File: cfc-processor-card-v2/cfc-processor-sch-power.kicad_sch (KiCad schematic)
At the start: 91 parts, among them Q1 DMP2240UDM, Q2 PMV45EN, Q3 DMP3050LVT-7, Q4 DMP3050LVT-7, Q5 PMV45EN, U1 MAX7310ATE+, U2 MIC842LYC5, U3 MIC842LYC5, U4 TS5A21366, U5 MAX4211FETE, U6 TPS62112

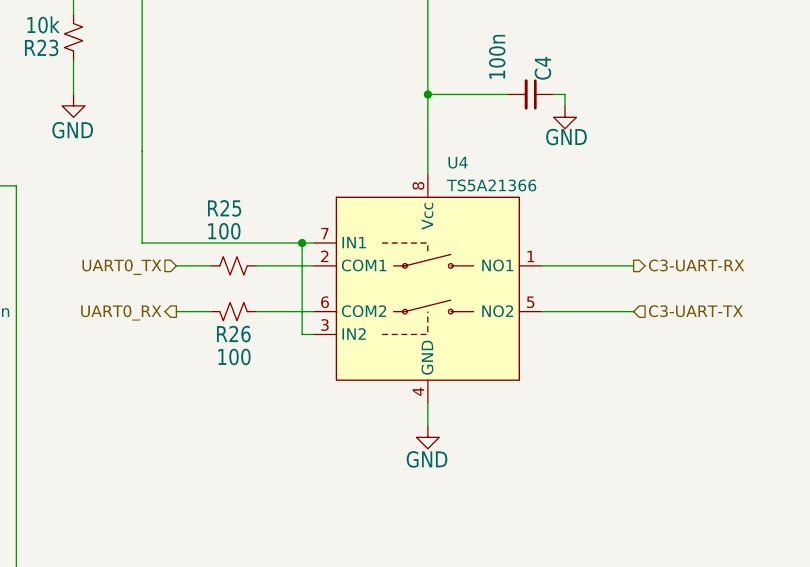
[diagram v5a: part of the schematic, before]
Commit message: Update
Changed passive component footprints to 0603 no silk c. Fixed OPD UART termination resistor on cfc processor card. Added low temp co and tolerance resistor for NTC  thermistor tec voltage divider.
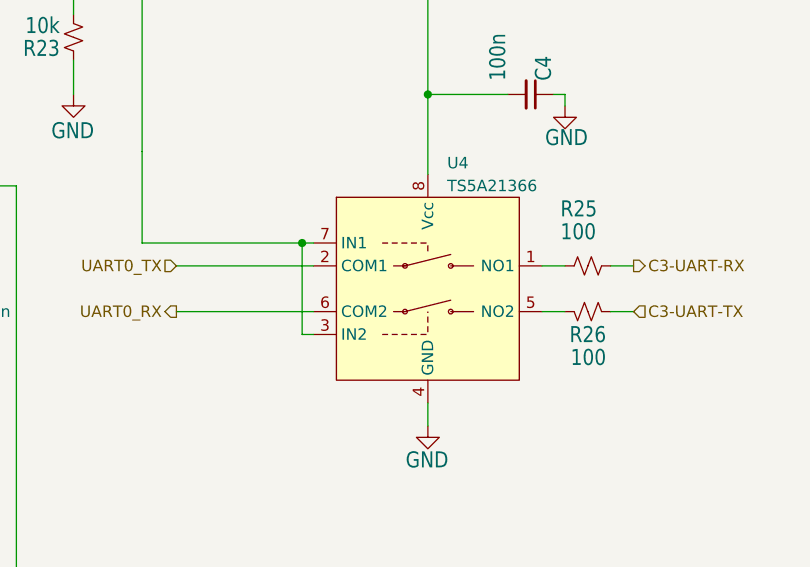
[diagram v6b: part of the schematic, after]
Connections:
- net C3-UART-RX: now also R25.1; no longer U4.1 (NO1)
- net C3-UART-TX: now also R26.2; no longer U4.5 (NO2)
- net UART0_RX: now also U4.6 (COM2); no longer R26.1
- net UART0_TX: now also U4.2 (COM1); no longer R25.2
- new net: R25.2, U4.1 (NO1)
- new net: R26.1, U4.5 (NO2)
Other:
- moved on the sheet: R25, R26
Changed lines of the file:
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@@
 	(wire
 		(pts
+			(xy 226.06 168.91) (xy 228.6 168.91)
+		)
+		(stroke
+			(width 0)
+			(type default)
+		)
+	)
+	(wire
+		(pts
 			(xy 68.58 48.26) (xy 71.12 48.26)
 		)
@@
 	(wire
 		(pts
+			(xy 226.06 173.99) (xy 228.6 173.99)
+		)
+		(stroke
+			(width 0)
+			(type default)
+		)
+	)
+	(wire
+		(pts
 			(xy 358.14 50.8) (xy 365.76 50.8)
 		)
@@
 	(wire
 		(pts
-			(xy 186.69 168.91) (xy 193.04 168.91)
-		)
-		(stroke
-			(width 0)
-			(type default)
-		)
-	)
-	(wire
-		(pts
 			(xy 320.04 60.96) (xy 332.74 60.96)
 		)
@@
 	(wire
 		(pts
-			(xy 186.69 173.99) (xy 193.04 173.99)
-		)
-		(stroke
-			(width 0)
-			(type default)
-		)
-	)
-	(wire
-		(pts
 			(xy 340.36 60.96) (xy 342.9 60.96)
 		)
@@
 	(wire
 		(pts
-			(xy 218.44 173.99) (xy 228.6 173.99)
+			(xy 177.8 173.99) (xy 193.04 173.99)
+		)
+		(stroke
+			(width 0)
+			(type default)
+		)
+	)
+	(wire
+		(pts
+			(xy 218.44 173.99) (xy 220.98 173.99)
 		)
 		(stroke
@@
 	(wire
 		(pts
-			(xy 177.8 168.91) (xy 181.61 168.91)
-		)
-		(stroke
-			(width 0)
-			(type default)
-		)
-	)
-	(wire
-		(pts
 			(xy 298.45 191.77) (xy 298.45 201.93)
 		)
@@
 	(wire
 		(pts
-			(xy 218.44 168.91) (xy 228.6 168.91)
+			(xy 218.44 168.91) (xy 220.98 168.91)
 		)
 		(stroke
@@
 	(wire
 		(pts
-			(xy 177.8 173.99) (xy 181.61 173.99)
-		)
-		(stroke
-			(width 0)
-			(type default)
-		)
-	)
-	(wire
-		(pts
 			(xy 283.21 59.69) (xy 283.21 53.34)
 		)
@@
 	(wire
 		(pts
+			(xy 177.8 168.91) (xy 193.04 168.91)
+		)
+		(stroke
+			(width 0)
+			(type default)
+		)
+	)
+	(wire
+		(pts
 			(xy 259.08 66.04) (xy 259.08 67.31)
 		)
@@
 	(symbol
 		(lib_id "Device:R_Small_US")
-		(at 184.15 173.99 90)
+		(at 223.52 173.99 90)
 		(mirror x)
 		(unit 1)
@@
 		(dnp no)
 		(property "Reference" "R26"
-			(at 186.182 175.514 90)
+			(at 225.552 175.514 90)
 			(show_name no)
 			(do_not_autoplace no)
@@
 		)
 		(property "Value" "100"
-			(at 186.182 178.054 90)
+			(at 225.552 178.054 90)
 			(show_name no)
 			(do_not_autoplace no)
@@
 		)
 		(property "Footprint" "oresat-passives:0603-C-NOSILK"
-			(at 184.15 173.99 0)
+			(at 223.52 173.99 0)
 			(hide yes)
 			(show_name no)
@@
 		)
 		(property "Datasheet" "https://www.seielect.com/catalog/sei-rmcf_rmcp.pdf"
-			(at 184.15 173.99 0)
+			(at 223.52 173.99 0)
 			(hide yes)
 			(show_name no)
@@
 		)
 		(property "Description" "Resistor, small US symbol"
-			(at 184.15 173.99 0)
+			(at 223.52 173.99 0)
 			(hide yes)
 			(show_name no)
@@
 		)
 		(property "DIS" "DigiKey"
-			(at 184.15 173.99 90)
+			(at 223.52 173.99 90)
 			(hide yes)
 			(show_name no)
@@
 		)
 		(property "DPN" "RMCF0603FT100RCT-ND"
-			(at 184.15 173.99 90)
+			(at 223.52 173.99 90)
 			(hide yes)
 			(show_name no)
@@
 		)
 		(property "MFR" "Stackpole Electronics Inc"
-			(at 184.15 173.99 90)
+			(at 223.52 173.99 90)
 			(hide yes)
 			(show_name no)
@@
 		)
 		(property "MPN" "RMCF0603FT100R"
-			(at 184.15 173.99 90)
+			(at 223.52 173.99 90)
 			(hide yes)
 			(show_name no)
@@
 	(symbol
 		(lib_id "Device:R_Small_US")
-		(at 184.15 168.91 270)
+		(at 223.52 168.91 270)
 		(unit 1)
 		(body_style 1)
@@
 		(dnp no)
 		(property "Reference" "R25"
-			(at 181.102 161.544 90)
+			(at 220.472 161.544 90)
 			(show_name no)
 			(do_not_autoplace no)
@@
 		)
 		(property "Value" "100"
-			(at 181.102 164.084 90)
+			(at 220.472 164.084 90)
 			(show_name no)
 			(do_not_autoplace no)
@@
 		)
 		(property "Footprint" "oresat-passives:0603-C-NOSILK"
-			(at 184.15 168.91 0)
+			(at 223.52 168.91 0)
 			(hide yes)
 			(show_name no)
@@
 		)
 		(property "Datasheet" "https://www.seielect.com/catalog/sei-rmcf_rmcp.pdf"
-			(at 184.15 168.91 0)
+			(at 223.52 168.91 0)
 			(hide yes)
 			(show_name no)
@@
 		)
 		(property "Description" "Resistor, small US symbol"
-			(at 184.15 168.91 0)
+			(at 223.52 168.91 0)
 			(hide yes)
 			(show_name no)
@@
 		)
 		(property "DIS" "DigiKey"
-			(at 184.15 168.91 90)
+			(at 223.52 168.91 90)
 			(hide yes)
 			(show_name no)
@@
 		)
 		(property "DPN" "RMCF0603FT100RCT-ND"
-			(at 184.15 168.91 90)
+			(at 223.52 168.91 90)
 			(hide yes)
 			(show_name no)
@@
 		)
 		(property "MFR" "Stackpole Electronics Inc"
-			(at 184.15 168.91 90)
+			(at 223.52 168.91 90)
 			(hide yes)
 			(show_name no)
@@
 		)
 		(property "MPN" "RMCF0603FT100R"
-			(at 184.15 168.91 90)
+			(at 223.52 168.91 90)
 			(hide yes)
 			(show_name no)

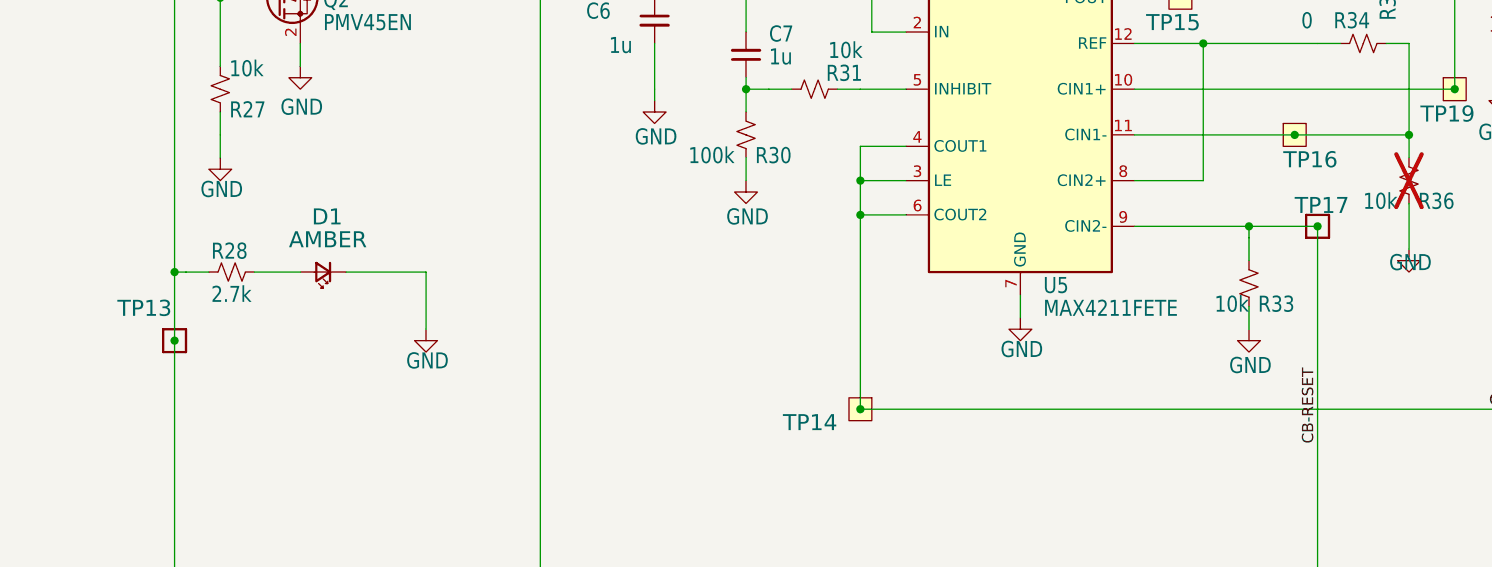
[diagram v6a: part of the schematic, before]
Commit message: update
Changed a couple of test points on OPD to through hole test points. Added tables to DRV8212 on sensor schematic+ other visual improvements to processor schematic.
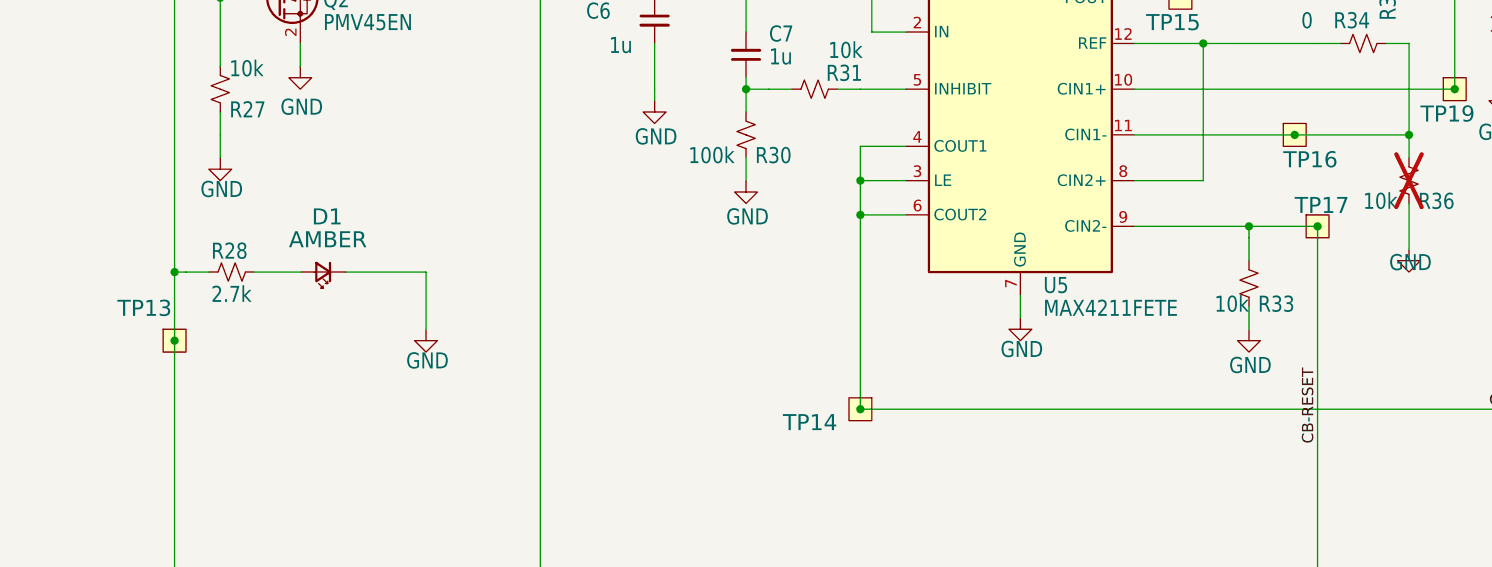
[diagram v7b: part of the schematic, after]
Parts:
- TP13, TP17: footprint cfc-card:2MM-TEST-POINT -> oresat-misc:TestPoint-0.75mm-th; symbol cfc-card-eagle-import:TEST-POINT -> oresat-misc:Test-Point-0.75mm-th
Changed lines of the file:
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@@
 	)
 	(symbol
-		(lib_id "cfc-card-eagle-import:TEST-POINT")
+		(lib_id "oresat-misc:Test-Point-0.75mm-th")
 		(at 332.74 81.28 0)
 		(unit 1)
@@
 			)
 		)
-		(property "Footprint" "cfc-card:2MM-TEST-POINT"
-			(at 332.74 81.28 0)
+		(property "Footprint" "oresat-misc:TestPoint-0.75mm-th"
+			(at 332.74 71.12 0)
 			(hide yes)
 			(show_name no)
@@
 			)
 		)
-		(property "Description" ""
+		(property "Description" "0.75 mm TH test point; good for scope probes and jumpers"
 			(at 332.74 81.28 0)
 			(hide yes)
@@
 	)
 	(symbol
-		(lib_id "cfc-card-eagle-import:TEST-POINT")
+		(lib_id "oresat-misc:Test-Point-0.75mm-th")
 		(at 205.74 93.98 0)
 		(unit 1)
@@
 			)
 		)
-		(property "Footprint" "cfc-card:2MM-TEST-POINT"
-			(at 205.74 93.98 0)
+		(property "Footprint" "oresat-misc:TestPoint-0.75mm-th"
+			(at 205.74 83.82 0)
 			(hide yes)
 			(show_name no)
@@
 			)
 		)
-		(property "Description" ""
+		(property "Description" "0.75 mm TH test point; good for scope probes and jumpers"
 			(at 205.74 93.98 0)
 			(hide yes)
